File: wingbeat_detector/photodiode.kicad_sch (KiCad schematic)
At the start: 1 part

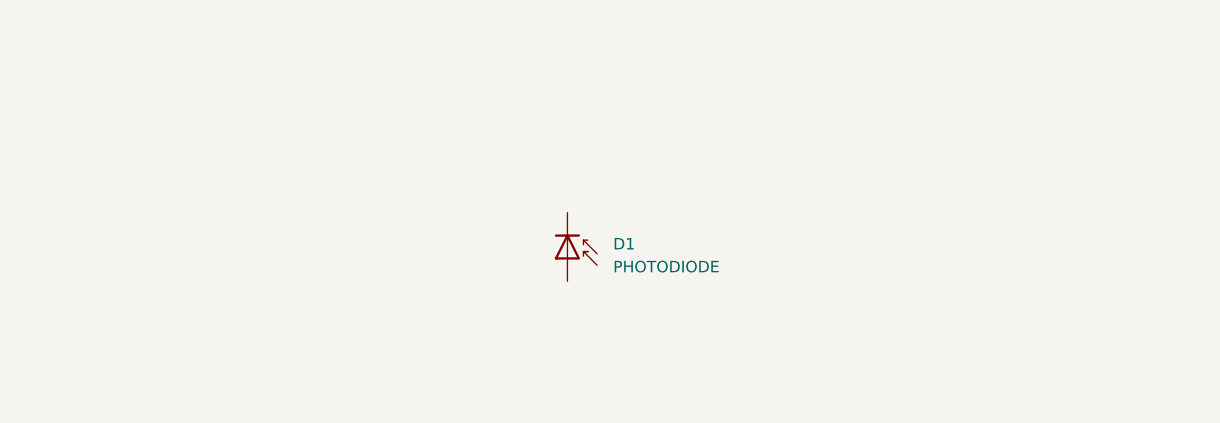
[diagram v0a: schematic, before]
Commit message: Add mosfet and opa381
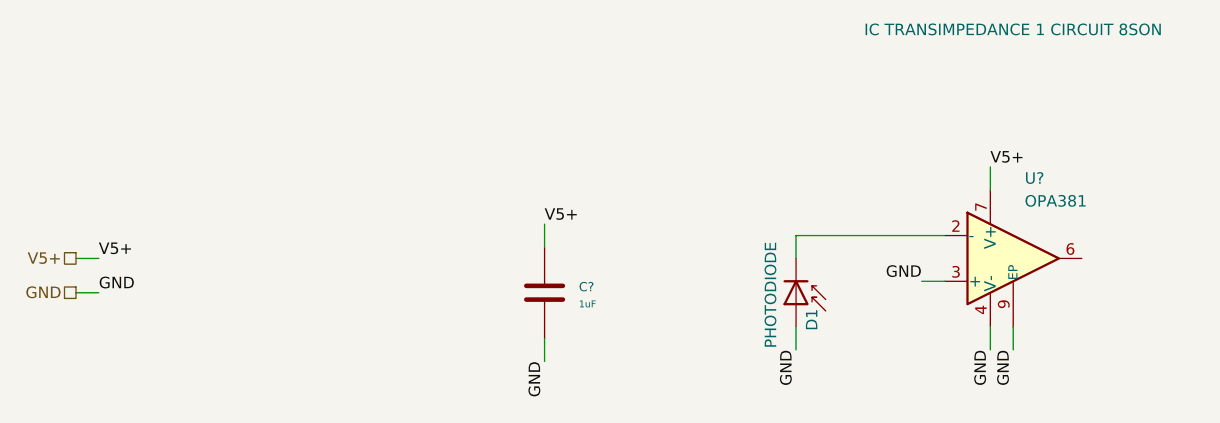
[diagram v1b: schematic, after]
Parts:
- added C?: 1uF, Janelia:C_0402_1005Metric, symbol Janelia:C_1uF_0402
- added U?: OPA381, Janelia:VSON-8-1EP_3x3mm_P0.65mm_EP1.65x2.4mm, symbol Janelia:OPA381
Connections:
- net at D1.1 (K): now also U?.2 (-)
- net GND: now reaches D1.2 (A)
- net GND: now also C?.2, U?.3 (+), U?.4 (V-), U?.9 (EP)
- new net V5+: C?.1, U?.7 (V+)
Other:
- moved on the sheet: D1
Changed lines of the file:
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@@
 (kicad_sch (version 20230121) (generator eeschema)
   (paper "A4")
-  (symbol (lib_id "Janelia:PHOTODIODE_940nm_RADIAL_RA_SMD_BRIGHT") (at 110.49 83.82 270) (unit 1)
+  (wire (pts (xy 55.88 83.82) (xy 58.42 83.82))
+    (stroke (width 0) (type default))
+  )
+  (wire (pts (xy 135.89 83.82) (xy 135.89 81.28))
+    (stroke (width 0) (type default))
+  )
+  (wire (pts (xy 160.02 91.44) (xy 160.02 93.98))
+    (stroke (width 0) (type default))
+  )
+  (wire (pts (xy 135.89 91.44) (xy 135.89 93.98))
+    (stroke (width 0) (type default))
+  )
+  (wire (pts (xy 107.95 92.71) (xy 107.95 95.25))
+    (stroke (width 0) (type default))
+  )
+  (wire (pts (xy 157.48 91.44) (xy 157.48 93.98))
+    (stroke (width 0) (type default))
+  )
+  (wire (pts (xy 135.89 81.28) (xy 152.4 81.28))
+    (stroke (width 0) (type default))
+  )
+  (wire (pts (xy 55.88 87.63) (xy 58.42 87.63))
+    (stroke (width 0) (type default))
+  )
+  (wire (pts (xy 157.48 76.2) (xy 157.48 73.66))
+    (stroke (width 0) (type default))
+  )
+  (wire (pts (xy 152.4 86.36) (xy 149.86 86.36))
+    (stroke (width 0) (type default))
+  )
+  (wire (pts (xy 107.95 82.55) (xy 107.95 80.01))
+    (stroke (width 0) (type default))
+  )
+  (label "V5+" (at 157.48 73.66 0) (fields_autoplaced)
+    (effects (font (size 1.27 1.27)) (justify left bottom))
+  )
+  (label "GND" (at 135.89 93.98 270) (fields_autoplaced)
+    (effects (font (size 1.27 1.27)) (justify right bottom))
+  )
+  (label "V5+" (at 107.95 80.01 0) (fields_autoplaced)
+    (effects (font (size 1.27 1.27)) (justify left bottom))
+  )
+  (label "GND" (at 107.95 95.25 270) (fields_autoplaced)
+    (effects (font (size 1.27 1.27)) (justify right bottom))
+  )
+  (label "GND" (at 58.42 87.63 0) (fields_autoplaced)
+    (effects (font (size 1.27 1.27)) (justify left bottom))
+  )
+  (label "GND" (at 157.48 93.98 270) (fields_autoplaced)
+    (effects (font (size 1.27 1.27)) (justify right bottom))
+  )
+  (label "GND" (at 149.86 86.36 180) (fields_autoplaced)
+    (effects (font (size 1.27 1.27)) (justify right bottom))
+  )
+  (label "V5+" (at 58.42 83.82 0) (fields_autoplaced)
+    (effects (font (size 1.27 1.27)) (justify left bottom))
+  )
+  (label "GND" (at 160.02 93.98 270) (fields_autoplaced)
+    (effects (font (size 1.27 1.27)) (justify right bottom))
+  )
+  (hierarchical_label "V5+" (shape passive) (at 55.88 83.82 180) (fields_autoplaced)
+    (effects (font (size 1.27 1.27)) (justify right))
+  )
+  (hierarchical_label "GND" (shape passive) (at 55.88 87.63 180) (fields_autoplaced)
+    (effects (font (size 1.27 1.27)) (justify right))
+  )
+  (symbol (lib_id "Janelia:C_1uF_0402") (at 107.95 87.63 0) (unit 1)
     (in_bom yes) (on_board yes) (dnp no) (fields_autoplaced)
-    (property "Reference" "D1" (at 115.57 82.2325 90)
+    (property "Reference" "C?" (at 111.76 86.995 0)
+      (effects (font (size 1.016 1.016)) (justify left))
+    )
+    (property "Value" "1uF" (at 111.76 88.9 0)
+      (effects (font (size 0.762 0.762)) (justify left))
+    )
+    (property "Footprint" "Janelia:C_0402_1005Metric" (at 108.9152 91.44 0)
+      (effects (font (size 0.762 0.762)) hide)
+    )
+    (property "Datasheet" "" (at 107.95 87.63 0)
+      (effects (font (size 1.524 1.524)) hide)
+    )
+    (property "Vendor" "Digi-Key" (at 110.49 82.55 0)
+      (effects (font (size 1.524 1.524)) hide)
+    )
+    (property "Vendor Part Number" "1276-6796-1-ND" (at 113.03 80.01 0)
+      (effects (font (size 1.524 1.524)) hide)
+    )
+    (property "Description" "CAP CER 1UF 35V X5R" (at 115.57 77.47 0)
+      (effects (font (size 1.524 1.524)) hide)
+    )
+    (property "Package" "0402" (at 107.95 87.63 0)
+      (effects (font (size 1.27 1.27)) hide)
+    )
+    (property "Manufacturer" "Samsung Electro-Mechanics" (at 107.95 87.63 0)
+      (effects (font (size 1.27 1.27)) hide)
+    )
+    (property "Manufacturer Part Number" "CL05A105KL5NRNC" (at 107.95 87.63 0)
+      (effects (font (size 1.27 1.27)) hide)
+    )
+    (pin "1")
+    (pin "2")
+    (instances
+      (project "wingbeat_detector"
+        (path "/cc457ebc-4af6-4663-b19f-8cb38f061cb4/6f9841bf-b0ef-48ff-bf2c-2bd611c72bf3"
+          (reference "C?") (unit 1)
+        )
+      )
+    )
+  )
+  (symbol (lib_id "Janelia:OPA381") (at 160.02 83.82 0) (unit 1)
+    (in_bom yes) (on_board yes) (dnp no)
+    (property "Reference" "U?" (at 161.29 74.93 0)
       (effects (font (size 1.27 1.27)) (justify left))
     )
-    (property "Value" "PHOTODIODE" (at 115.57 84.7725 90)
+    (property "Value" "OPA381" (at 161.29 77.47 0)
       (effects (font (size 1.27 1.27)) (justify left))
     )
-    (property "Footprint" "Janelia:PHOTODIODE_RADIAL_RA_SMD_BRIGHT" (at 123.19 83.82 0)
+    (property "Footprint" "Janelia:VSON-8-1EP_3x3mm_P0.65mm_EP1.65x2.4mm" (at 160.02 60.96 0)
       (effects (font (size 1.27 1.27)) hide)
     )
-    (property "Datasheet" "~" (at 110.49 82.55 0)
+    (property "Datasheet" "" (at 160.02 66.04 0)
       (effects (font (size 1.27 1.27)) hide)
     )
-    (property "Manufacturer" "American Bright Optoelectronics Corporation" (at 125.73 83.82 0)
+    (property "Manufacturer" "Texas Instruments" (at 160.02 55.88 0)
       (effects (font (size 1.27 1.27)) hide)
     )
-    (property "Manufacturer Part Number" "BPD-BQDA38V-FZ04" (at 118.11 83.82 0)
+    (property "Manufacturer Part Number" "OPA381AIDRBT" (at 160.02 50.8 0)
       (effects (font (size 1.27 1.27)) hide)
     )
-    (property "Vendor" "Digi-Key" (at 105.41 83.82 0)
+    (property "Vendor" "Digi-Key" (at 160.02 63.5 0)
       (effects (font (size 1.27 1.27)) hide)
     )
-    (property "Vendor Part Number" "BPD-BQDA38V-FZ04CT-ND" (at 115.57 83.82 0)
+    (property "Vendor Part Number" "296-17363-1-ND" (at 160.02 53.34 0)
       (effects (font (size 1.27 1.27)) hide)
     )
-    (property "Description" "SENSOR PHOTODIODE RADIAL" (at 120.65 83.82 0)
+    (property "Description" "IC TRANSIMPEDANCE 1 CIRCUIT 8SON" (at 160.02 58.42 0)
+      (effects (font (size 1.27 1.27)))
+    )
+    (pin "7")
+    (pin "9")
+    (pin "6")
+    (pin "2")
+    (pin "3")
+    (pin "4")
+    (instances
+      (project "wingbeat_detector"
+        (path "/cc457ebc-4af6-4663-b19f-8cb38f061cb4/6f9841bf-b0ef-48ff-bf2c-2bd611c72bf3"
+          (reference "U?") (unit 1)
+        )
+      )
+    )
+  )
+  (symbol (lib_id "Janelia:PHOTODIODE_940nm_RADIAL_RA_SMD_BRIGHT") (at 135.89 88.9 270) (unit 1)
+    (in_bom yes) (on_board yes) (dnp no)
+    (property "Reference" "D1" (at 137.668 89.408 0)
+      (effects (font (size 1.27 1.27)) (justify left))
+    )
+    (property "Value" "PHOTODIODE" (at 133.096 87.884 0)
+      (effects (font (size 1.27 1.27)))
+    )
+    (property "Footprint" "Janelia:PHOTODIODE_RADIAL_RA_SMD_BRIGHT" (at 148.59 88.9 0)
+      (effects (font (size 1.27 1.27)) hide)
+    )
+    (property "Datasheet" "~" (at 135.89 87.63 0)
+      (effects (font (size 1.27 1.27)) hide)
+    )
+    (property "Manufacturer" "American Bright Optoelectronics Corporation" (at 151.13 88.9 0)
+      (effects (font (size 1.27 1.27)) hide)
+    )
+    (property "Manufacturer Part Number" "BPD-BQDA38V-FZ04" (at 143.51 88.9 0)
+      (effects (font (size 1.27 1.27)) hide)
+    )
+    (property "Vendor" "Digi-Key" (at 130.81 88.9 0)
+      (effects (font (size 1.27 1.27)) hide)
+    )
+    (property "Vendor Part Number" "BPD-BQDA38V-FZ04CT-ND" (at 140.97 88.9 0)
+      (effects (font (size 1.27 1.27)) hide)
+    )
+    (property "Description" "SENSOR PHOTODIODE RADIAL" (at 146.05 88.9 0)
       (effects (font (size 1.27 1.27)) hide)
     )
@@
         )
         (path "/cc457ebc-4af6-4663-b19f-8cb38f061cb4/6f9841bf-b0ef-48ff-bf2c-2bd611c72bf3"
-          (reference "D1") (unit 1)
+          (reference "D?") (unit 1)
         )
       )

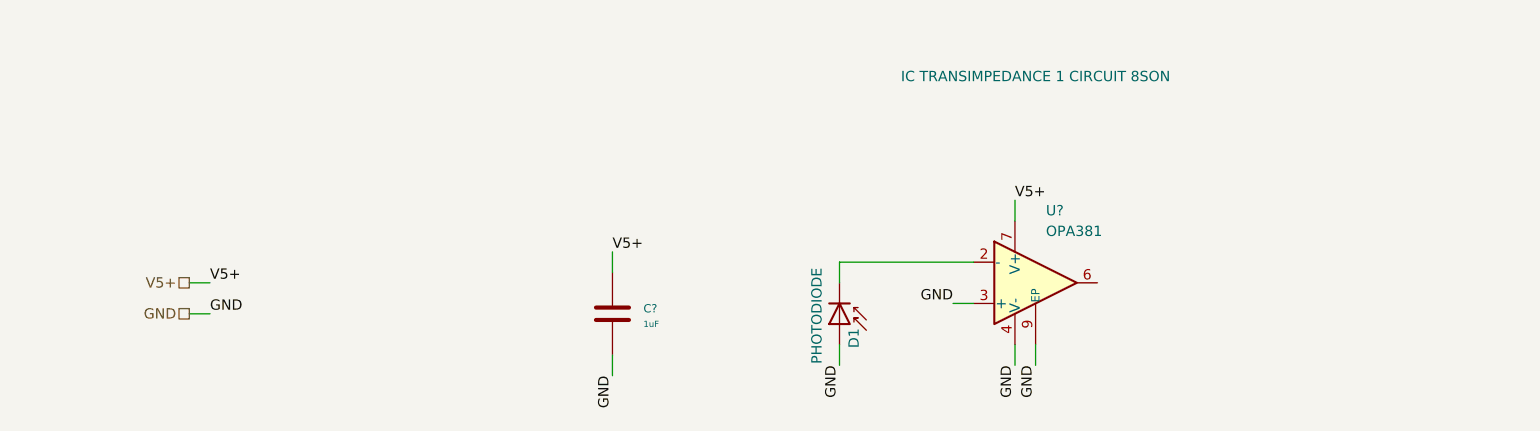
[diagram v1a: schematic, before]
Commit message: Remove connectors schematic sheet
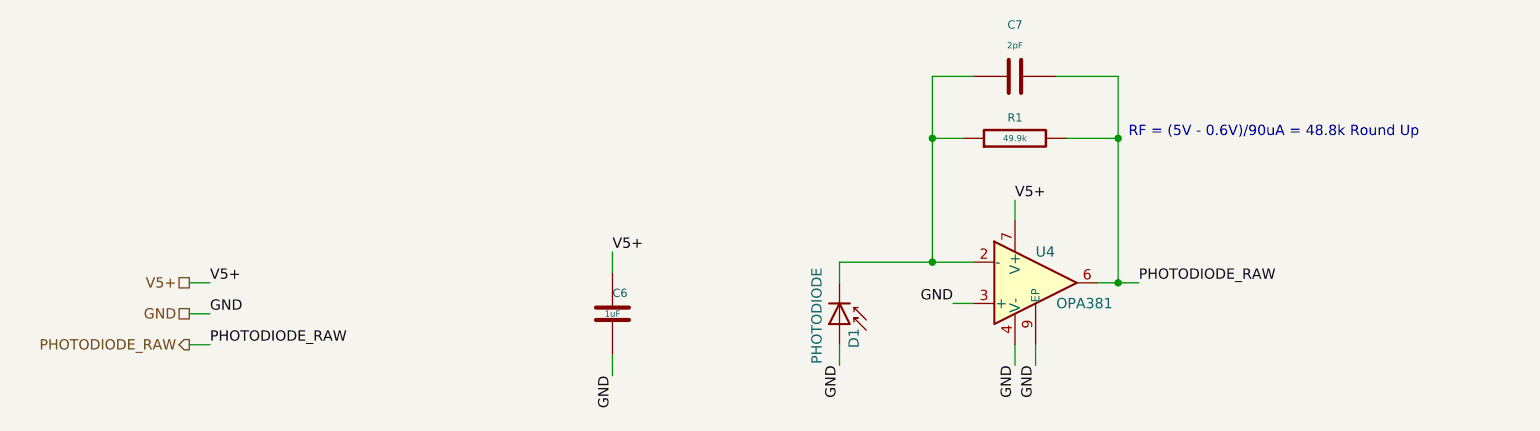
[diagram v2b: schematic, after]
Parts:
- added C7: 2pF, Janelia:C_0402_1005Metric, symbol Janelia:C_2pF_0402
- added R1: 49.9k, Janelia:R_0402_1005Metric, symbol Janelia:R_49.9k_0402
- gave numbers to parts that had none: 2
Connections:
- net at D1.1 (K), U4.2 (-): now also C7.1, R1.1
- net PHOTODIODE_RAW: now reaches U4.6
- net PHOTODIODE_RAW: now also C7.2, R1.2
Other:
- note added: "RF = (5V - 0.6V)/90uA = 48.8k Round Up"
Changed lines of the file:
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@@
 (kicad_sch (version 20230121) (generator eeschema)
   (paper "A4")
+  (junction (at 170.18 66.04) (diameter 0) (color 0 0 0 0)
+  )
+  (junction (at 147.32 66.04) (diameter 0) (color 0 0 0 0)
+  )
+  (junction (at 170.18 83.82) (diameter 0) (color 0 0 0 0)
+  )
+  (junction (at 147.32 81.28) (diameter 0) (color 0 0 0 0)
+  )
   (wire (pts (xy 55.88 83.82) (xy 58.42 83.82))
     (stroke (width 0) (type default))
@@
     (stroke (width 0) (type default))
   )
+  (wire (pts (xy 170.18 58.42) (xy 170.18 66.04))
+    (stroke (width 0) (type default))
+  )
+  (wire (pts (xy 170.18 83.82) (xy 172.72 83.82))
+    (stroke (width 0) (type default))
+  )
   (wire (pts (xy 160.02 91.44) (xy 160.02 93.98))
     (stroke (width 0) (type default))
   )
+  (wire (pts (xy 147.32 81.28) (xy 152.4 81.28))
+    (stroke (width 0) (type default))
+  )
+  (wire (pts (xy 170.18 83.82) (xy 170.18 66.04))
+    (stroke (width 0) (type default))
+  )
   (wire (pts (xy 135.89 91.44) (xy 135.89 93.98))
     (stroke (width 0) (type default))
   )
+  (wire (pts (xy 55.88 91.44) (xy 58.42 91.44))
+    (stroke (width 0) (type default))
+  )
+  (wire (pts (xy 163.83 66.04) (xy 170.18 66.04))
+    (stroke (width 0) (type default))
+  )
   (wire (pts (xy 107.95 92.71) (xy 107.95 95.25))
     (stroke (width 0) (type default))
   )
+  (wire (pts (xy 167.64 83.82) (xy 170.18 83.82))
+    (stroke (width 0) (type default))
+  )
+  (wire (pts (xy 162.56 58.42) (xy 170.18 58.42))
+    (stroke (width 0) (type default))
+  )
+  (wire (pts (xy 151.13 66.04) (xy 147.32 66.04))
+    (stroke (width 0) (type default))
+  )
   (wire (pts (xy 157.48 91.44) (xy 157.48 93.98))
     (stroke (width 0) (type default))
   )
-  (wire (pts (xy 135.89 81.28) (xy 152.4 81.28))
+  (wire (pts (xy 135.89 81.28) (xy 147.32 81.28))
     (stroke (width 0) (type default))
   )
@@
     (stroke (width 0) (type default))
   )
+  (wire (pts (xy 147.32 66.04) (xy 147.32 58.42))
+    (stroke (width 0) (type default))
+  )
   (wire (pts (xy 152.4 86.36) (xy 149.86 86.36))
     (stroke (width 0) (type default))
   )
+  (wire (pts (xy 147.32 58.42) (xy 152.4 58.42))
+    (stroke (width 0) (type default))
+  )
+  (wire (pts (xy 147.32 66.04) (xy 147.32 81.28))
+    (stroke (width 0) (type default))
+  )
   (wire (pts (xy 107.95 82.55) (xy 107.95 80.01))
     (stroke (width 0) (type default))
   )
+  (text "RF = (5V - 0.6V)/90uA = 48.8k Round Up" (at 171.45 66.04 0)
+    (effects (font (size 1.27 1.27)) (justify left bottom))
+  )
   (label "V5+" (at 157.48 73.66 0) (fields_autoplaced)
     (effects (font (size 1.27 1.27)) (justify left bottom))
@@
     (effects (font (size 1.27 1.27)) (justify left bottom))
   )
+  (label "PHOTODIODE_RAW" (at 172.72 83.82 0) (fields_autoplaced)
+    (effects (font (size 1.27 1.27)) (justify left bottom))
+  )
   (label "GND" (at 107.95 95.25 270) (fields_autoplaced)
     (effects (font (size 1.27 1.27)) (justify right bottom))
@@
     (effects (font (size 1.27 1.27)) (justify left bottom))
   )
+  (label "PHOTODIODE_RAW" (at 58.42 91.44 0) (fields_autoplaced)
+    (effects (font (size 1.27 1.27)) (justify left bottom))
+  )
   (label "GND" (at 160.02 93.98 270) (fields_autoplaced)
     (effects (font (size 1.27 1.27)) (justify right bottom))
+  )
+  (hierarchical_label "PHOTODIODE_RAW" (shape output) (at 55.88 91.44 180) (fields_autoplaced)
+    (effects (font (size 1.27 1.27)) (justify right))
   )
   (hierarchical_label "V5+" (shape passive) (at 55.88 83.82 180) (fields_autoplaced)
@@
     (effects (font (size 1.27 1.27)) (justify right))
   )
+  (symbol (lib_id "Janelia:R_49.9k_0402") (at 157.48 66.04 90) (unit 1)
+    (in_bom yes) (on_board yes) (dnp no)
+    (property "Reference" "R1" (at 157.48 63.5 90)
+      (effects (font (size 1.016 1.016)))
+    )
+    (property "Value" "49.9k" (at 157.48 66.04 90)
+      (effects (font (size 0.762 0.762)))
+    )
+    (property "Footprint" "Janelia:R_0402_1005Metric" (at 157.48 67.818 90)
+      (effects (font (size 0.762 0.762)) hide)
+    )
+    (property "Datasheet" "" (at 157.48 64.008 90)
+      (effects (font (size 0.762 0.762)))
+    )
+    (property "Vendor" "Digi-Key" (at 154.94 61.468 90)
+      (effects (font (size 1.524 1.524)) hide)
+    )
+    (property "Vendor Part Number" "P49.9KLCT-ND" (at 152.4 58.928 90)
+      (effects (font (size 1.524 1.524)) hide)
+    )
+    (property "Description" "RES SMD 49.9K OHM 1% 1/10W" (at 149.86 56.388 90)
+      (effects (font (size 1.524 1.524)) hide)
+    )
+    (property "Package" "0402" (at 157.48 66.04 0)
+      (effects (font (size 1.27 1.27)) hide)
+    )
+    (property "Manufacturer" "Panasonic Electronic Components" (at 157.48 66.04 0)
+      (effects (font (size 1.27 1.27)) hide)
+    )
+    (property "Manufacturer Part Number" "ERJ-2RKF4992X" (at 157.48 66.04 0)
+      (effects (font (size 1.27 1.27)) hide)
+    )
+    (pin "1")
+    (pin "2")
+    (instances
+      (project "wingbeat_detector"
+        (path "/cc457ebc-4af6-4663-b19f-8cb38f061cb4/6f9841bf-b0ef-48ff-bf2c-2bd611c72bf3"
+          (reference "R1") (unit 1)
+        )
+      )
+    )
+  )
   (symbol (lib_id "Janelia:C_1uF_0402") (at 107.95 87.63 0) (unit 1)
-    (in_bom yes) (on_board yes) (dnp no) (fields_autoplaced)
-    (property "Reference" "C?" (at 111.76 86.995 0)
+    (in_bom yes) (on_board yes) (dnp no)
+    (property "Reference" "C6" (at 107.95 85.09 0)
       (effects (font (size 1.016 1.016)) (justify left))
     )
-    (property "Value" "1uF" (at 111.76 88.9 0)
-      (effects (font (size 0.762 0.762)) (justify left))
+    (property "Value" "1uF" (at 107.95 87.63 0)
+      (effects (font (size 0.762 0.762)))
     )
     (property "Footprint" "Janelia:C_0402_1005Metric" (at 108.9152 91.44 0)
@@
       (project "wingbeat_detector"
         (path "/cc457ebc-4af6-4663-b19f-8cb38f061cb4/6f9841bf-b0ef-48ff-bf2c-2bd611c72bf3"
-          (reference "C?") (unit 1)
+          (reference "C6") (unit 1)
+        )
+      )
+    )
+  )
+  (symbol (lib_id "Janelia:C_2pF_0402") (at 157.48 58.42 90) (unit 1)
+    (in_bom yes) (on_board yes) (dnp no) (fields_autoplaced)
+    (property "Reference" "C7" (at 157.48 52.07 90)
+      (effects (font (size 1.016 1.016)))
+    )
+    (property "Value" "2pF" (at 157.48 54.61 90)
+      (effects (font (size 0.762 0.762)))
+    )
+    (property "Footprint" "Janelia:C_0402_1005Metric" (at 161.29 57.4548 0)
+      (effects (font (size 0.762 0.762)) hide)
+    )
+    (property "Datasheet" "" (at 157.48 58.42 0)
+      (effects (font (size 1.524 1.524)) hide)
+    )
+    (property "Vendor" "Digi-Key" (at 152.4 55.88 0)
+      (effects (font (size 1.524 1.524)) hide)
+    )
+    (property "Vendor Part Number" "445-5572-1-ND" (at 149.86 53.34 0)
+      (effects (font (size 1.524 1.524)) hide)
+    )
+    (property "Description" "CAP CER 2PF 50V C0G" (at 147.32 50.8 0)
+      (effects (font (size 1.524 1.524)) hide)
+    )
+    (property "Package" "0402" (at 157.48 58.42 0)
+      (effects (font (size 1.27 1.27)) hide)
+    )
+    (property "Manufacturer" "TDK Corporation" (at 157.48 58.42 0)
+      (effects (font (size 1.27 1.27)) hide)
+    )
+    (property "Manufacturer Part Number" "CGA2B2C0G1H020C050BA" (at 157.48 58.42 0)
+      (effects (font (size 1.27 1.27)) hide)
+    )
+    (pin "1")
+    (pin "2")
+    (instances
+      (project "wingbeat_detector"
+        (path "/cc457ebc-4af6-4663-b19f-8cb38f061cb4/6f9841bf-b0ef-48ff-bf2c-2bd611c72bf3"
+          (reference "C7") (unit 1)
         )
       )
@@
   (symbol (lib_id "Janelia:OPA381") (at 160.02 83.82 0) (unit 1)
     (in_bom yes) (on_board yes) (dnp no)
-    (property "Reference" "U?" (at 161.29 74.93 0)
+    (property "Reference" "U4" (at 160.02 80.01 0)
       (effects (font (size 1.27 1.27)) (justify left))
     )
-    (property "Value" "OPA381" (at 161.29 77.47 0)
+    (property "Value" "OPA381" (at 162.56 86.36 0)
       (effects (font (size 1.27 1.27)) (justify left))
     )
@@
     )
     (property "Description" "IC TRANSIMPEDANCE 1 CIRCUIT 8SON" (at 160.02 58.42 0)
-      (effects (font (size 1.27 1.27)))
+      (effects (font (size 1.27 1.27)) hide)
     )
     (pin "7")
@@
       (project "wingbeat_detector"
         (path "/cc457ebc-4af6-4663-b19f-8cb38f061cb4/6f9841bf-b0ef-48ff-bf2c-2bd611c72bf3"
-          (reference "U?") (unit 1)
+          (reference "U4") (unit 1)
         )
       )
@@
         )
         (path "/cc457ebc-4af6-4663-b19f-8cb38f061cb4/6f9841bf-b0ef-48ff-bf2c-2bd611c72bf3"
-          (reference "D?") (unit 1)
-        )
-      )
+          (reference "D1") (unit 1)
+        )
+      )
